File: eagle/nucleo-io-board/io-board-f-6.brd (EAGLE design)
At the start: 100 x 80 mm, 166 parts, among them IC1 LM2574N-5.0, IC2 CAN-TXR-SO8, J1 DCJ0202, P1 9-15V DC, U1 CAN-TXR-PDIP, U10 TC4426/28, U11 74AHCT595N, U13 74AHCT595N, U2 AP1509-50, U3 74HC166, U4 74HC166, U5 TC4426/28, U6 LM324N, U7 TC4426/28, U8 TC4426/28, U9 LM324N, X1 RJ45-JACK, X2 RJ45-JACK, X3 M08-SCREW, X4 M08-SCREW, X6 M08-SCREW, X7 PORTD, X8 PORTE

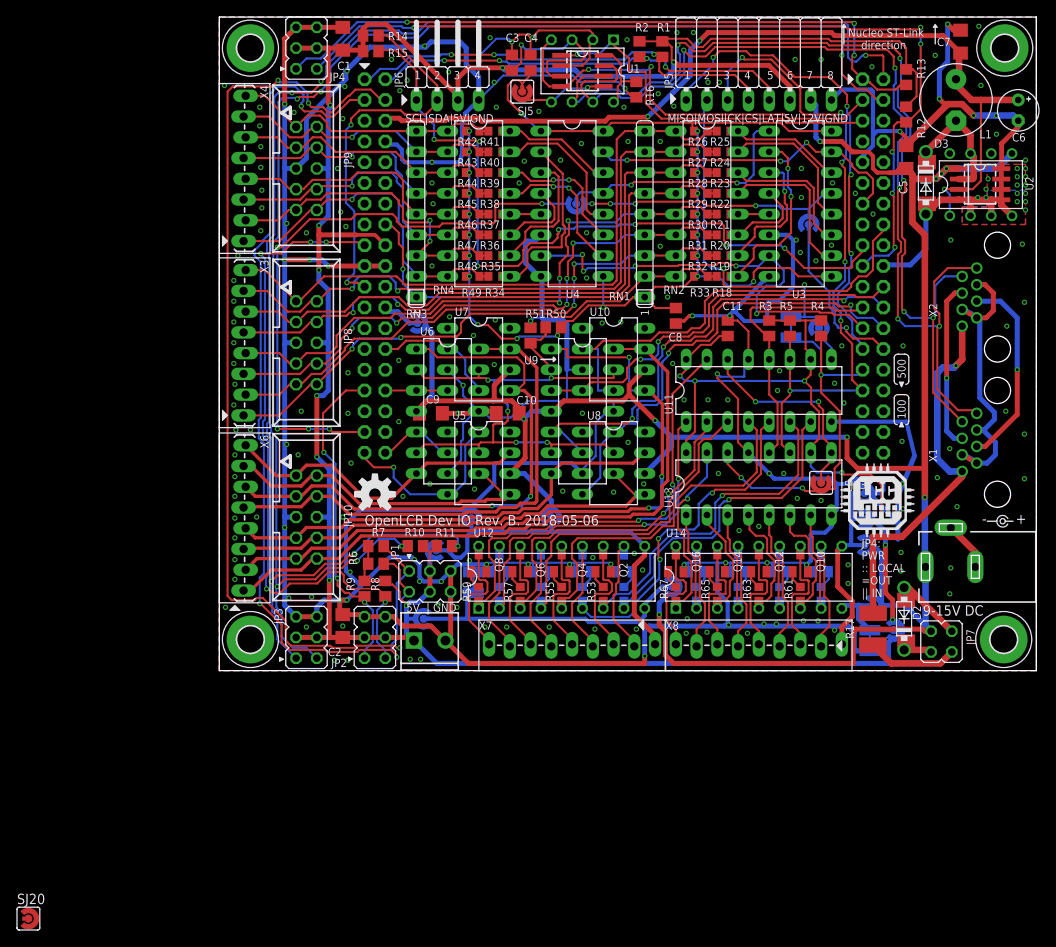
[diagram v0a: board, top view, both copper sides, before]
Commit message: New revisions to fix comments from the review process.
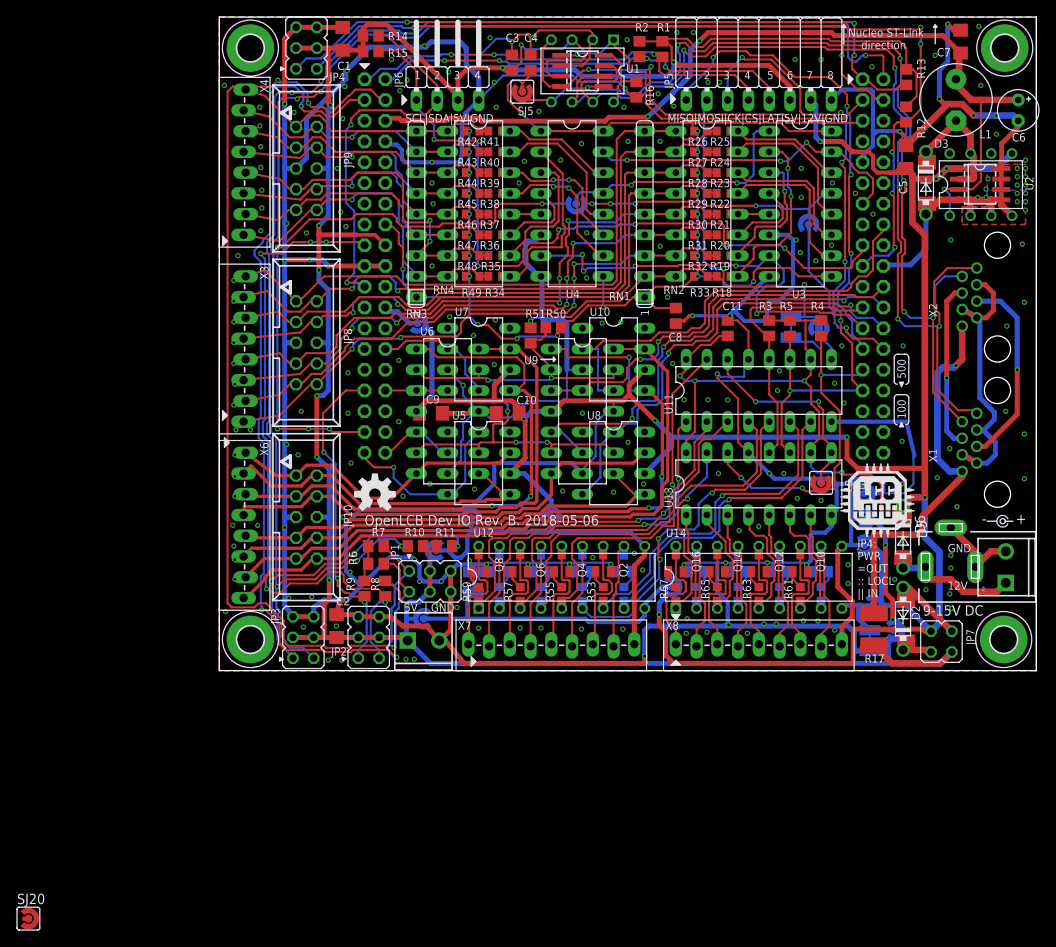
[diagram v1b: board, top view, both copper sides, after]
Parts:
- added D5: (no value), diode:DO41-7.6
- added D6: DIODEDO-214AA-NODOC, trainlib:DO214AA-NODOC
- added X9: (no value), SPCoast:SCREWTERMINAL-3.5MM-2_LOCK
- U10, U5, U7, U8: value TC4426/28 -> TC4427
- moved X7 2.54 mm to (30.5, 3.10)
- moved X6 0.91 mm to (3.10, 26.7)
- moved JP2 0.76 mm to (18.3, 4.06)
- moved X3 0.76 mm to (3.10, 48.3)
- moved X4 0.76 mm to (3.10, 71.1)
- moved X5 0.76 mm to (23.2, 3.68)
- moved C2 0.76 mm to (14.4, 5.46)
- moved JP3 0.38 mm to (10.3, 4.06)
- moved D2 0.13 mm to (83.7, 6.35)
- moved R17 0.13 mm to (80.1, 5.08)
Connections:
- new net N$4: D5.A, D6.A, J1.1, X9.1
- net +12V: now also D5.C, D6.C; no longer J1.1
- net GND: now also X9.2
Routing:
- net N$4: track 0.00 -> 16.5 mm
- net +12V: track 268.7 -> 274.8 mm
- net GND: track 758.7 -> 757.5 mm, vias 222 -> 225
- net TOUT8: track 80.0 -> 81.1 mm
- net N$99: track 14.8 -> 13.7 mm
- net N$93: track 15.7 -> 14.6 mm
- net N$75: track 14.8 -> 13.7 mm
- net N$95: track 14.8 -> 13.7 mm
- net N$91: track 14.8 -> 13.7 mm
- net LPOWB: track 45.3 -> 44.3 mm
- net PWR_POS: track 46.0 -> 47.0 mm
- net N$87: track 15.8 -> 14.8 mm
- net TOUT4: track 62.4 -> 63.3 mm
- net N$97: track 15.5 -> 14.6 mm
- net N$101: track 15.5 -> 14.6 mm
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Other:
- board text added: "GND 12V"
- board text added: "JP4: PWR =OUT :: LOCL || IN"
- board text removed: "JP4: PWR :: LOCAL =OUT || IN"
